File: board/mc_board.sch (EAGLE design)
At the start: 16 parts, among them IC1 MEGA8-P, Q1 16MHz

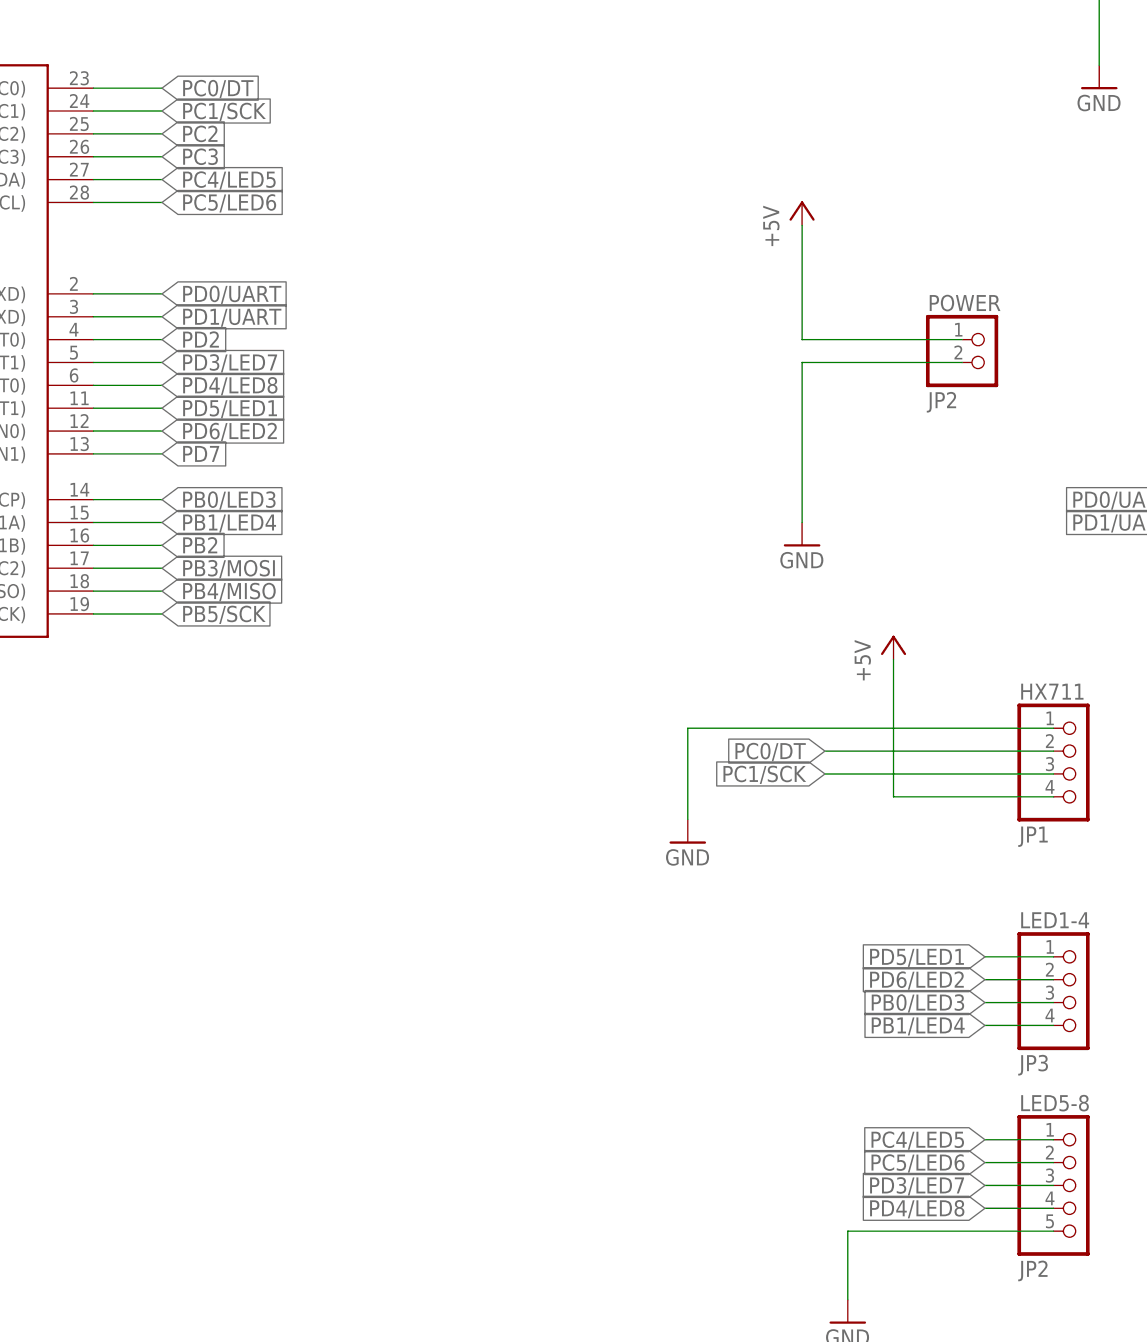
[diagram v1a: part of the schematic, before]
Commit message: tweaked board layout, defined pins in led.c accordingly
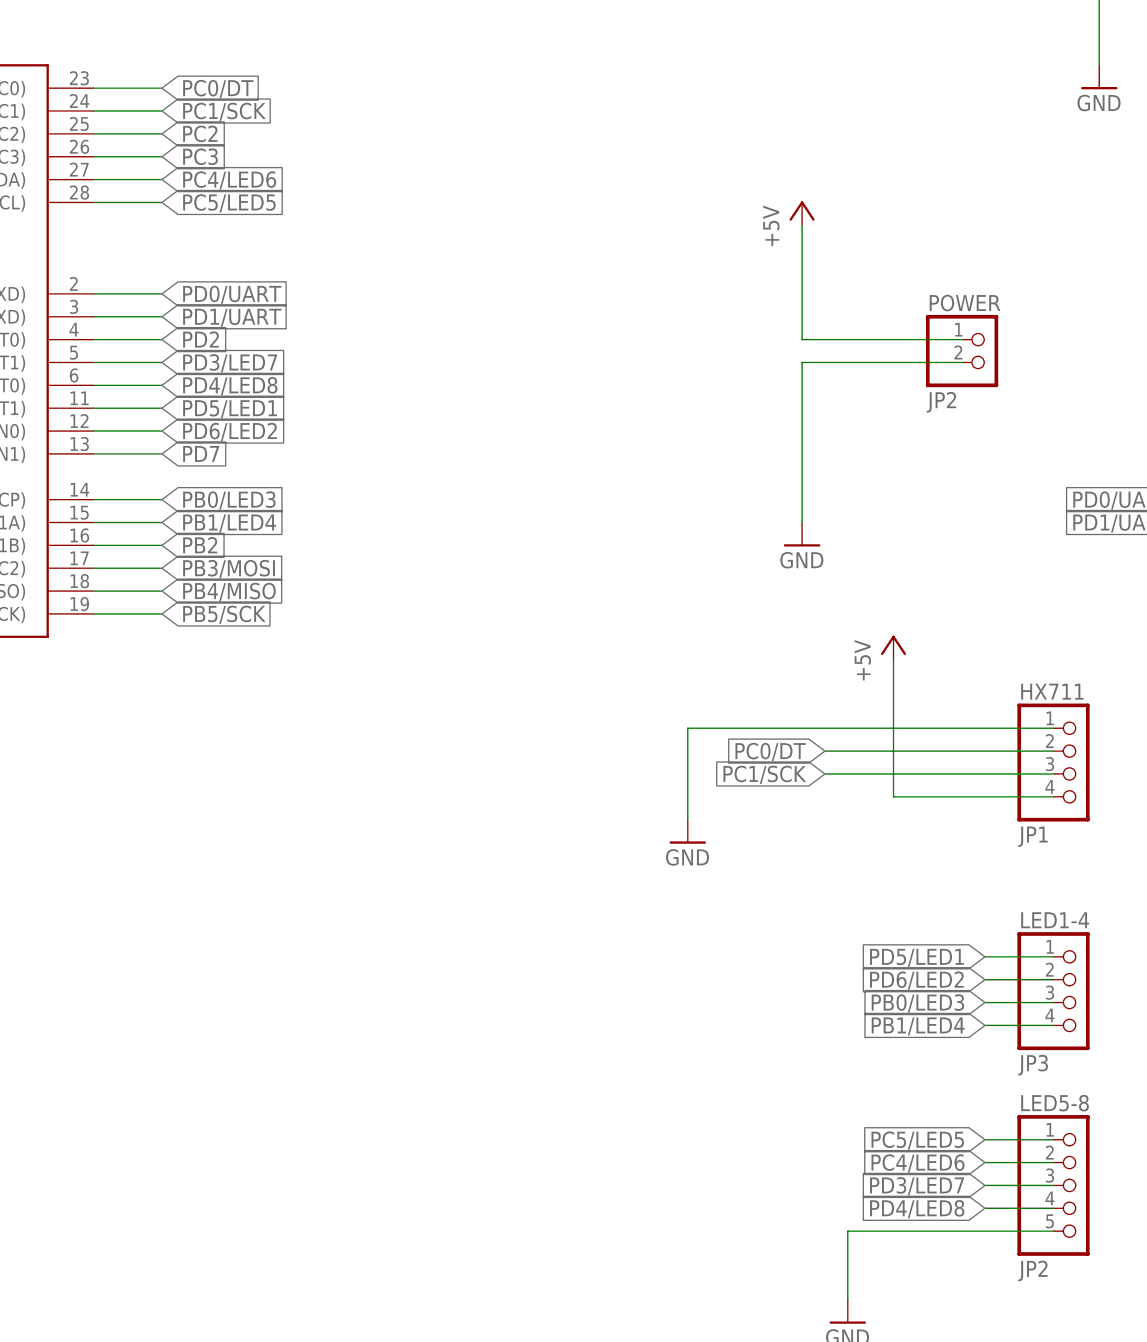
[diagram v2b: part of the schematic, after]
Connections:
- removed net PC4/LED5: IC1.PC4(ADC4/SDA), LED5-8.1
- removed net PC5/LED6: IC1.PC5(ADC5/SCL), LED5-8.2
- new net PC4/LED6: IC1.PC4(ADC4/SDA), LED5-8.2
- new net PC5/LED5: IC1.PC5(ADC5/SCL), LED5-8.1
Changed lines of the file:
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@@
-</segment>
-</net>
-<net name="PC4/LED5" class="0">
-<segment>
-<wire x1="233.68" y1="177.8" x2="241.3" y2="177.8" width="0.1524" layer="91"/>
-<pinref part="IC1" gate="G$1" pin="PC4(ADC4/SDA)"/>
-<label x="241.3" y="177.8" size="1.778" layer="95" xref="yes"/>
-</segment>
-<segment>
-<wire x1="340.36" y1="71.12" x2="332.74" y2="71.12" width="0.1524" layer="91"/>
-<pinref part="LED5-8" gate="A" pin="1"/>
-<label x="332.74" y="71.12" size="1.778" layer="95" rot="MR0" xref="yes"/>
-</segment>
-</net>
-<net name="PC5/LED6" class="0">
-<segment>
-<wire x1="233.68" y1="175.26" x2="241.3" y2="175.26" width="0.1524" layer="91"/>
-<pinref part="IC1" gate="G$1" pin="PC5(ADC5/SCL)"/>
-<label x="241.3" y="175.26" size="1.778" layer="95" xref="yes"/>
-</segment>
-<segment>
-<wire x1="340.36" y1="68.58" x2="332.74" y2="68.58" width="0.1524" layer="91"/>
-<pinref part="LED5-8" gate="A" pin="2"/>
-<label x="332.74" y="68.58" size="1.778" layer="95" rot="MR0" xref="yes"/>
 </segment>
 </net>
@@
 </segment>
 </net>
+<net name="PC5/LED5" class="0">
+<segment>
+<wire x1="233.68" y1="175.26" x2="241.3" y2="175.26" width="0.1524" layer="91"/>
+<pinref part="IC1" gate="G$1" pin="PC5(ADC5/SCL)"/>
+<label x="241.3" y="175.26" size="1.778" layer="95" xref="yes"/>
+</segment>
+<segment>
+<wire x1="340.36" y1="71.12" x2="332.74" y2="71.12" width="0.1524" layer="91"/>
+<pinref part="LED5-8" gate="A" pin="1"/>
+<label x="332.74" y="71.12" size="1.778" layer="95" rot="MR0" xref="yes"/>
+</segment>
+</net>
+<net name="PC4/LED6" class="0">
+<segment>
+<wire x1="340.36" y1="68.58" x2="332.74" y2="68.58" width="0.1524" layer="91"/>
+<pinref part="LED5-8" gate="A" pin="2"/>
+<label x="332.74" y="68.58" size="1.778" layer="95" rot="MR0" xref="yes"/>
+</segment>
+<segment>
+<wire x1="233.68" y1="177.8" x2="241.3" y2="177.8" width="0.1524" layer="91"/>
+<pinref part="IC1" gate="G$1" pin="PC4(ADC4/SDA)"/>
+<label x="241.3" y="177.8" size="1.778" layer="95" xref="yes"/>
+</segment>
+</net>

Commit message: improved board layout
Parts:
- removed LED5-8: JP2, pinhead:PINHD-1X5
- added GND: Gnd, pinhead:PINHD-1X1
- added LED5-8JO: JP2, pinhead:PINHD-1X4
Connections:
- net GND: now also GND.1; no longer LED5-8.5
- net PC4/LED6: now also LED5-8JO.2; no longer LED5-8.2
- net PC5/LED5: now also LED5-8JO.1; no longer LED5-8.1
- net PD3/LED7: now also LED5-8JO.3; no longer LED5-8.3
- net PD4/LED8: now also LED5-8JO.4; no longer LED5-8.4
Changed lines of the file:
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@@
 <part name="GND6" library="supply1" deviceset="GND" device=""/>
 <part name="P+5" library="supply1" deviceset="+5V" device=""/>
-<part name="LED5-8" library="pinhead" deviceset="PINHD-1X5" device="" value="JP2"/>
 <part name="LED1-4" library="pinhead" deviceset="PINHD-1X4" device="" value="JP3"/>
 <part name="GND8" library="supply1" deviceset="GND" device=""/>
 <part name="UART" library="pinhead" deviceset="PINHD-1X2" device="" value="JP2"/>
+<part name="GND" library="pinhead" deviceset="PINHD-1X1" device="" value="Gnd"/>
+<part name="LED5-8JO" library="pinhead" deviceset="PINHD-1X4" device="" value="JP2"/>
 </parts>
 <sheets>
@@
 <instance part="GND6" gate="1" x="299.72" y="104.14"/>
 <instance part="P+5" gate="1" x="322.58" y="127"/>
-<instance part="LED5-8" gate="A" x="342.9" y="66.04"/>
 <instance part="LED1-4" gate="A" x="342.9" y="86.36"/>
-<instance part="GND8" gate="1" x="317.5" y="50.8"/>
+<instance part="GND8" gate="1" x="335.28" y="35.56"/>
 <instance part="UART" gate="G$1" x="370.84" y="139.7"/>
+<instance part="GND" gate="G$1" x="358.14" y="45.72"/>
+<instance part="LED5-8JO" gate="A" x="342.9" y="66.04"/>
 </instances>
 <busses>
@@
 </segment>
 <segment>
-<pinref part="LED5-8" gate="A" pin="5"/>
 <pinref part="GND8" gate="1" pin="GND"/>
-<wire x1="317.5" y1="53.34" x2="317.5" y2="60.96" width="0.1524" layer="91"/>
-<wire x1="317.5" y1="60.96" x2="340.36" y2="60.96" width="0.1524" layer="91"/>
+<pinref part="GND" gate="G$1" pin="1"/>
+<wire x1="335.28" y1="38.1" x2="335.28" y2="45.72" width="0.1524" layer="91"/>
+<wire x1="335.28" y1="45.72" x2="355.6" y2="45.72" width="0.1524" layer="91"/>
 </segment>
 </net>
@@
 <segment>
 <wire x1="340.36" y1="66.04" x2="332.74" y2="66.04" width="0.1524" layer="91"/>
-<pinref part="LED5-8" gate="A" pin="3"/>
 <label x="332.74" y="66.04" size="1.778" layer="95" rot="MR0" xref="yes"/>
+<pinref part="LED5-8JO" gate="A" pin="3"/>
 </segment>
 </net>
@@
 <segment>
 <wire x1="340.36" y1="63.5" x2="332.74" y2="63.5" width="0.1524" layer="91"/>
-<pinref part="LED5-8" gate="A" pin="4"/>
 <label x="332.74" y="63.5" size="1.778" layer="95" rot="MR0" xref="yes"/>
+<pinref part="LED5-8JO" gate="A" pin="4"/>
 </segment>
 </net>
@@
 <segment>
 <wire x1="340.36" y1="71.12" x2="332.74" y2="71.12" width="0.1524" layer="91"/>
-<pinref part="LED5-8" gate="A" pin="1"/>
 <label x="332.74" y="71.12" size="1.778" layer="95" rot="MR0" xref="yes"/>
+<pinref part="LED5-8JO" gate="A" pin="1"/>
 </segment>
 </net>
@@
 <segment>
 <wire x1="340.36" y1="68.58" x2="332.74" y2="68.58" width="0.1524" layer="91"/>
-<pinref part="LED5-8" gate="A" pin="2"/>
 <label x="332.74" y="68.58" size="1.778" layer="95" rot="MR0" xref="yes"/>
-</segment>
-<segment>
+<pinref part="LED5-8JO" gate="A" pin="2"/>
+</segment>
+<segment>

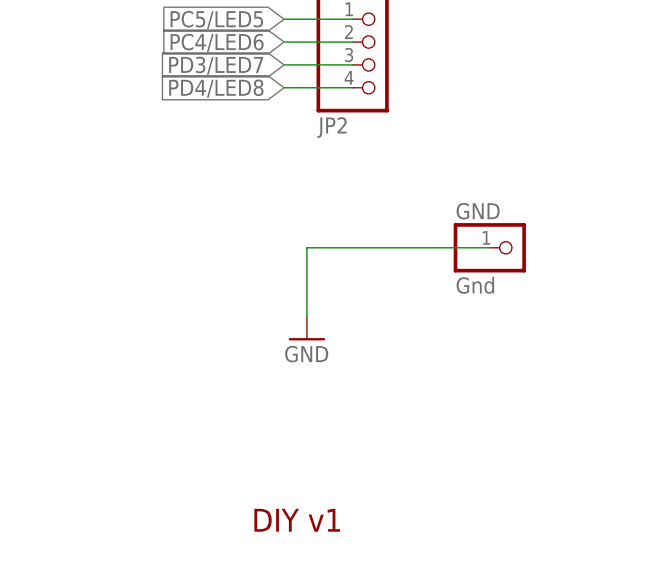
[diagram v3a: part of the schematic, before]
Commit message: removed gnd pin form board
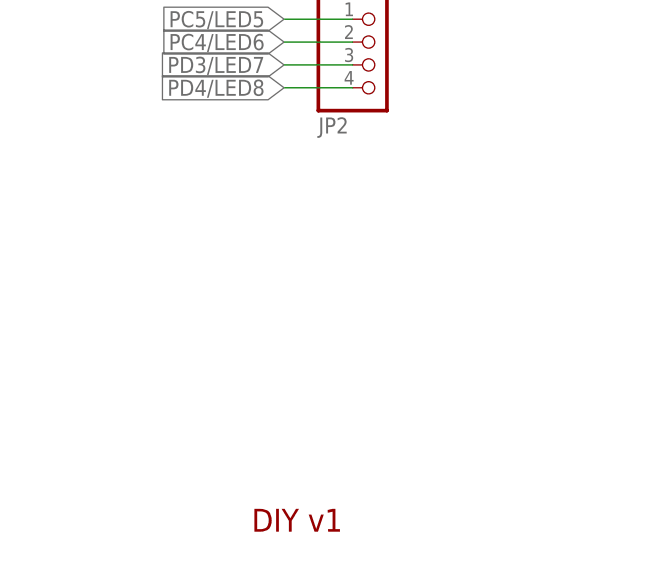
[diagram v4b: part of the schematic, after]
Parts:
- removed GND: Gnd, pinhead:PINHD-1X1
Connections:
- net GND: no longer GND.1
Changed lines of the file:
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@@
 <part name="P+5" library="supply1" deviceset="+5V" device=""/>
 <part name="LED1-4" library="pinhead" deviceset="PINHD-1X4" device="" value="JP3"/>
-<part name="GND8" library="supply1" deviceset="GND" device=""/>
 <part name="UART" library="pinhead" deviceset="PINHD-1X2" device="" value="JP2"/>
-<part name="GND" library="pinhead" deviceset="PINHD-1X1" device="" value="Gnd"/>
 <part name="LED5-8JO" library="pinhead" deviceset="PINHD-1X4" device="" value="JP2"/>
 </parts>
@@
 <instance part="P+5" gate="1" x="322.58" y="127"/>
 <instance part="LED1-4" gate="A" x="342.9" y="86.36"/>
-<instance part="GND8" gate="1" x="335.28" y="35.56"/>
 <instance part="UART" gate="G$1" x="370.84" y="139.7"/>
-<instance part="GND" gate="G$1" x="358.14" y="45.72"/>
 <instance part="LED5-8JO" gate="A" x="342.9" y="66.04"/>
 </instances>
@@
 <wire x1="299.72" y1="116.84" x2="299.72" y2="106.68" width="0.1524" layer="91"/>
 </segment>
-<segment>
-<pinref part="GND8" gate="1" pin="GND"/>
-<pinref part="GND" gate="G$1" pin="1"/>
-<wire x1="335.28" y1="38.1" x2="335.28" y2="45.72" width="0.1524" layer="91"/>
-<wire x1="335.28" y1="45.72" x2="355.6" y2="45.72" width="0.1524" layer="91"/>
-</segment>
 </net>

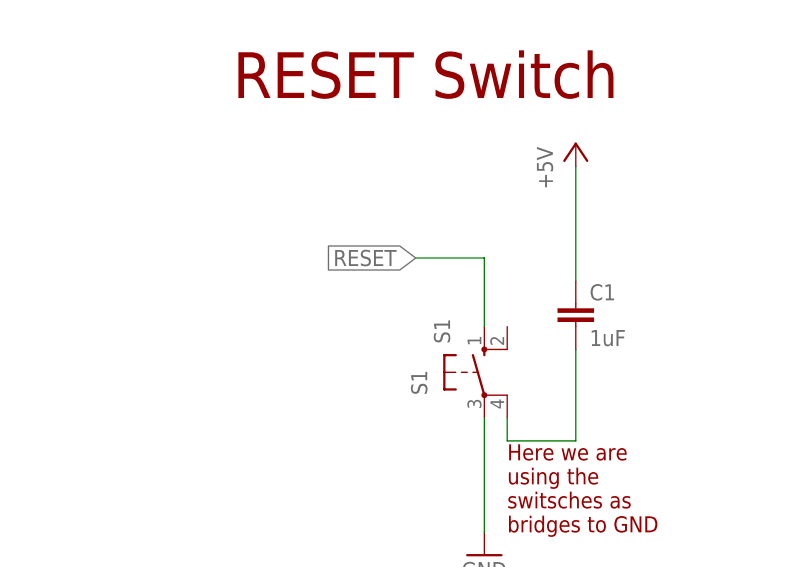
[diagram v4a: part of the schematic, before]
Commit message: changed reset button to normal button
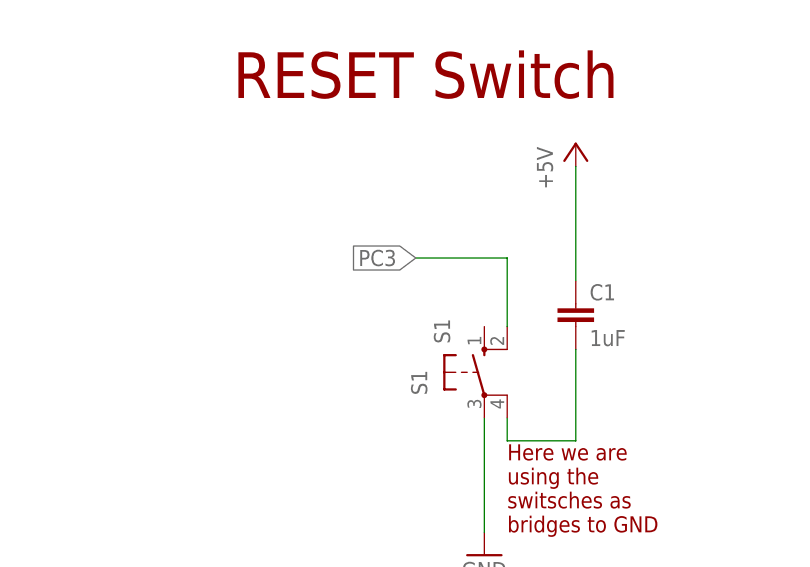
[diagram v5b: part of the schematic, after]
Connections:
- net PC3: now also S1.S1
- net RESET: no longer S1.S
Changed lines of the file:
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@@
 <label x="241.3" y="180.34" size="1.778" layer="95" xref="yes"/>
+</segment>
+<segment>
+<wire x1="165.1" y1="55.88" x2="154.94" y2="55.88" width="0.1524" layer="91"/>
+<label x="154.94" y="55.88" size="1.778" layer="95" rot="R180" xref="yes"/>
+<pinref part="S1" gate="1" pin="S1"/>
+<wire x1="165.1" y1="48.26" x2="165.1" y2="55.88" width="0.1524" layer="91"/>
 </segment>
 </net>
@@
 <net name="RESET" class="0">
 <segment>
-<wire x1="162.56" y1="48.26" x2="162.56" y2="55.88" width="0.1524" layer="91"/>
-<wire x1="162.56" y1="55.88" x2="154.94" y2="55.88" width="0.1524" layer="91"/>
-<label x="154.94" y="55.88" size="1.778" layer="95" rot="R180" xref="yes"/>
-<pinref part="S1" gate="1" pin="S"/>
-</segment>
-<segment>
 <wire x1="185.42" y1="187.96" x2="165.1" y2="187.96" width="0.1524" layer="91"/>
